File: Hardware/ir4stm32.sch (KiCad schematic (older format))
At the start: 62 parts

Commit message: feat: (irda_decode) Struct
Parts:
- added P3, P4, P5, P6, P7, P8, P9: CONN_01X03, symbol CONN_01X03
- added R10, R11, R12, R5, R6, R7, R9: 100, symbol R_Small
- gave numbers to parts that had none: 62
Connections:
- net 3V3: now also R4.2, R10.2, R11.2, R12.2, R5.2, R6.2, R7.2, R9.2
- net GND: now also P3.2 (P2), P4.2 (P2), P5.2 (P2), P6.2 (P2), P7.2 (P2), P8.2 (P2), P9.2 (P2)
- net IRIN_3: now reaches U2.10 (PC2/ADC12)
- net IRIN_3: now also P4.1 (P1)
- net IRIN_4: now reaches U2.11 (PC3/ADC13)
- net IRIN_4: now also P5.1 (P1)
- net IRIN_5: now reaches U2.37 (PC6)
- net IRIN_5: now also P6.1 (P1)
- net IRIN_6: now reaches U2.38 (PC7)
- net IRIN_6: now also P7.1 (P1)
- net IRIN_7: now reaches U2.39 (PC8)
- net IRIN_7: now also P8.1 (P1)
- net IRIN_8: now reaches U2.40 (PC9)
- net IRIN_8: now also P9.1 (P1)
- net IRIN_1: now reaches U2.8 (PC0/ADC10)
- net IRIN_1: now also P2.1 (P1)
- net IRIN_2: now reaches U2.9 (PC1/ADC11)
- net IRIN_2: now also P3.1 (P1)
- new net: P3.3 (P3), R5.1
- new net: P6.3 (P3), R9.1
- new net: P7.3 (P3), R10.1
- new net: P4.3 (P3), R6.1
- new net: P5.3 (P3), R7.1
- new net: P8.3 (P3), R11.1
- new net: P9.3 (P3), R12.1
- no-connect marks 4 -> 31
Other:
- note added: "Boot Options\n"
- note added: "Clock\n"
- note added: "ISP & Serial"
- note added: "IrDA Get"
- note added: "IrDA Send\n"
- note added: "Reset\n"
- moved on the sheet: C1, C2, P1, P2, R2, R4, Y1

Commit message: feat: Gerber files
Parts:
- C1, C10, C11, C12, C13, C14, C15, C16, C17, C18, C19, C2, C20, C3, C4, C5, C6, C7, C8, C9: footprint (none) -> Capacitors_SMD:C_0603
- D1, D2, D3, D4, D5, D6, D7, D8: footprint (none) -> Socket_Strips:Socket_Strip_Straight_1x02
- P1: footprint (none) -> Socket_Strips:Socket_Strip_Angled_1x04
- P2, P3, P4, P5, P6, P7, P8, P9: footprint (none) -> Socket_Strips:Socket_Strip_Straight_1x03
- Q1, Q2, Q3, Q4, Q5, Q6, Q7, Q8: footprint (none) -> TO_SOT_Packages_SMD:SOT-23
- R1, R10, R11, R12, R13, R14, R15, R16, R17, R18, R19, R2, R20, R21, R22, R23, R24, R25, R26, R27, R28, R3, R4, R5, R6, R7, R8, R9: footprint (none) -> Resistors_SMD:R_0603
- U1: value APE8865N-33-HF-3 -> XC6206P332MR; footprint SOT-23 -> TO_SOT_Packages_SMD:SOT-23
- U2: footprint (none) -> Housings_QFP:LQFP-64_10x10mm_Pitch0.5mm
- Y1: footprint (none) -> Crystals:SMD-5032

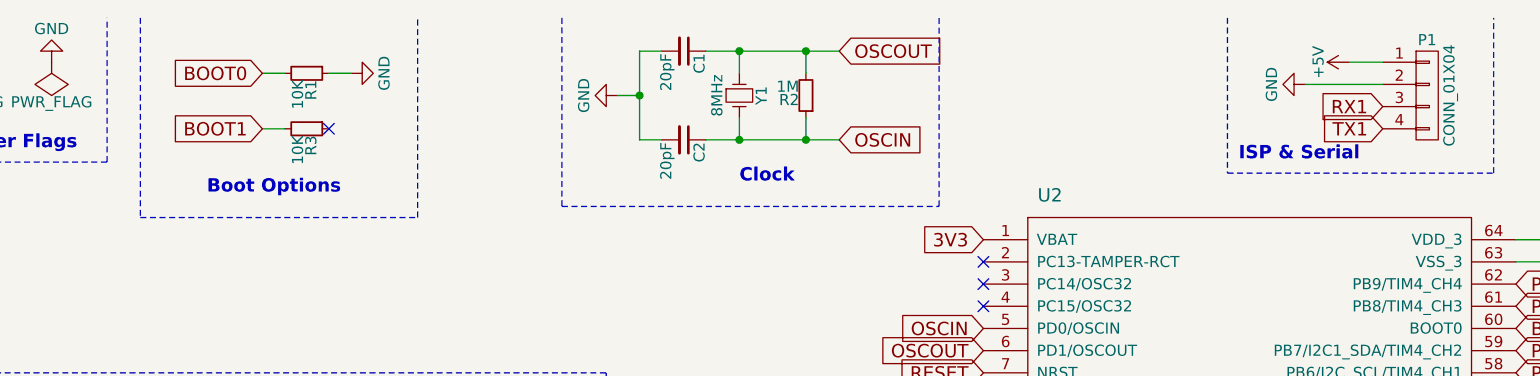
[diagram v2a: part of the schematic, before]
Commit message: fix: BOOT Options error
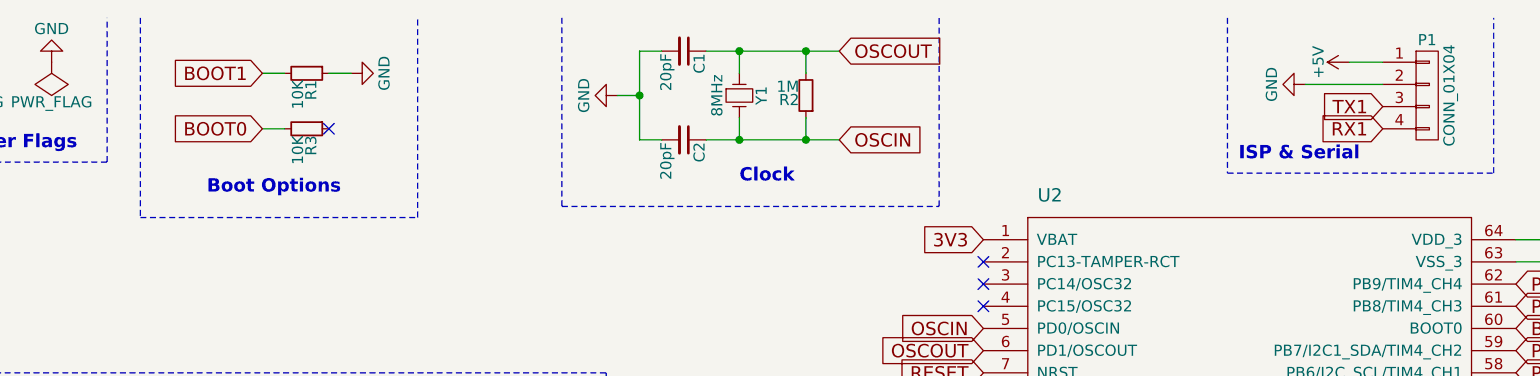
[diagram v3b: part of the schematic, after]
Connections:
- net BOOT0: now also R3.2; no longer R1.2
- net BOOT1: now also R1.2; no longer R3.2
- net RX1: now also P1.4 (P4); no longer P1.3 (P3)
- net TX1: now also P1.3 (P3); no longer P1.4 (P4)
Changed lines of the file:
@@
 $EndComp
 Text GLabel 4350 750  0    60   Input ~ 0
+BOOT1
+Text GLabel 4350 1000 0    60   Input ~ 0
 BOOT0
-Text GLabel 4350 1000 0    60   Input ~ 0
-BOOT1
 $Comp
 L GND #PWR014
@@
 $EndComp
 Text GLabel 9400 900  0    60   Input ~ 0
+TX1
+Text GLabel 9400 1000 0    60   Input ~ 0
 RX1
-Text GLabel 9400 1000 0    60   Input ~ 0
-TX1
 $Comp
 L Q_NPN_BEC Q5
